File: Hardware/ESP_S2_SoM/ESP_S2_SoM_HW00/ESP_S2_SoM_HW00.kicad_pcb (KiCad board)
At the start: 6 copper layers, 29.5 x 24.7 mm, 59 parts, among them J101 DF40C-60DP-0.4V(51), J102 Bare PCB USB C, SW401 SW_Push, SW402 SW_Push, U201 BQ24075RGTR, U301 MIC5528-3.3YMT-T5, U401 ESP32-S2FH4, Y601 Crystal_GND24_Small

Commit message: exported pcb fab
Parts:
- removed G***: LOGO, Component_lib:puma_logo_14mm
- removed the J101 at (136.0, 106.2)
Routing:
- net IO8: track 11.5 -> 10.7 mm
- net SPI7: track 4.86 -> 4.16 mm

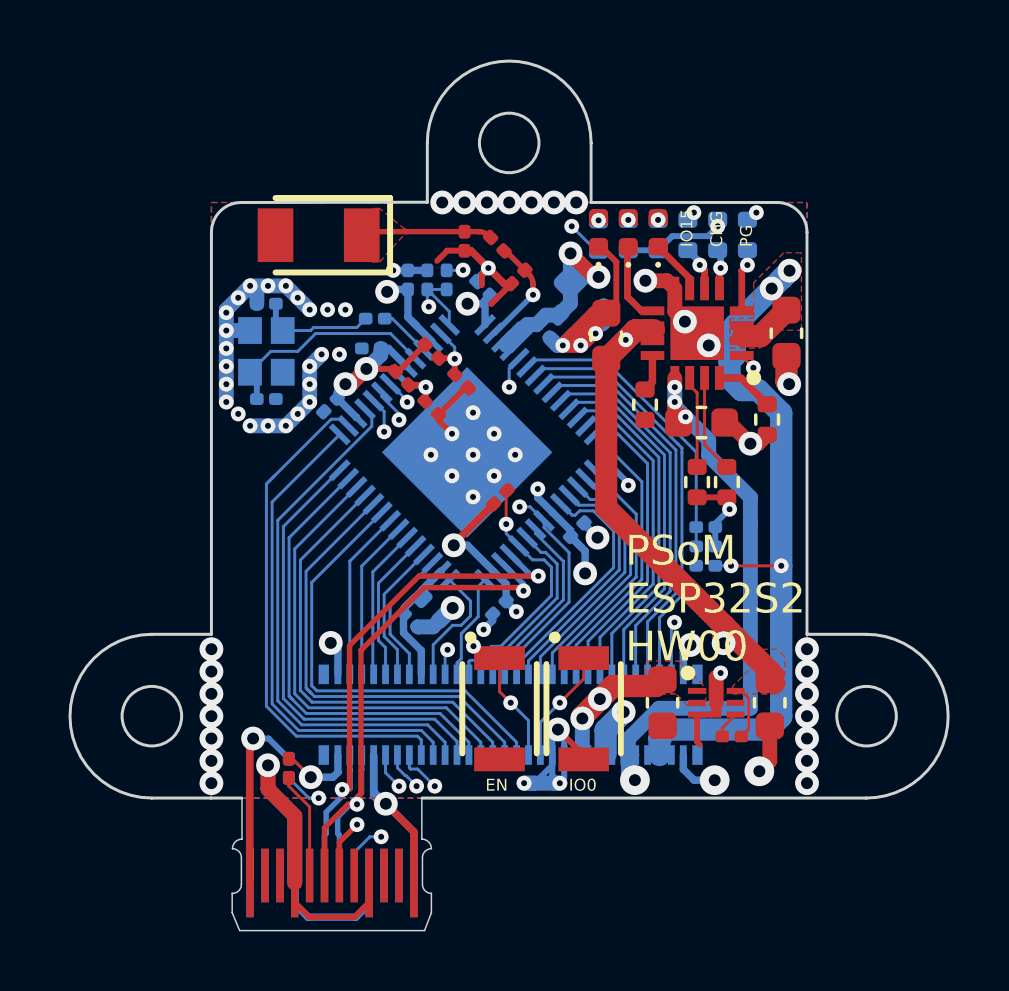
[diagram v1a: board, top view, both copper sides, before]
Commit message: updated prod files + holes are M1.6
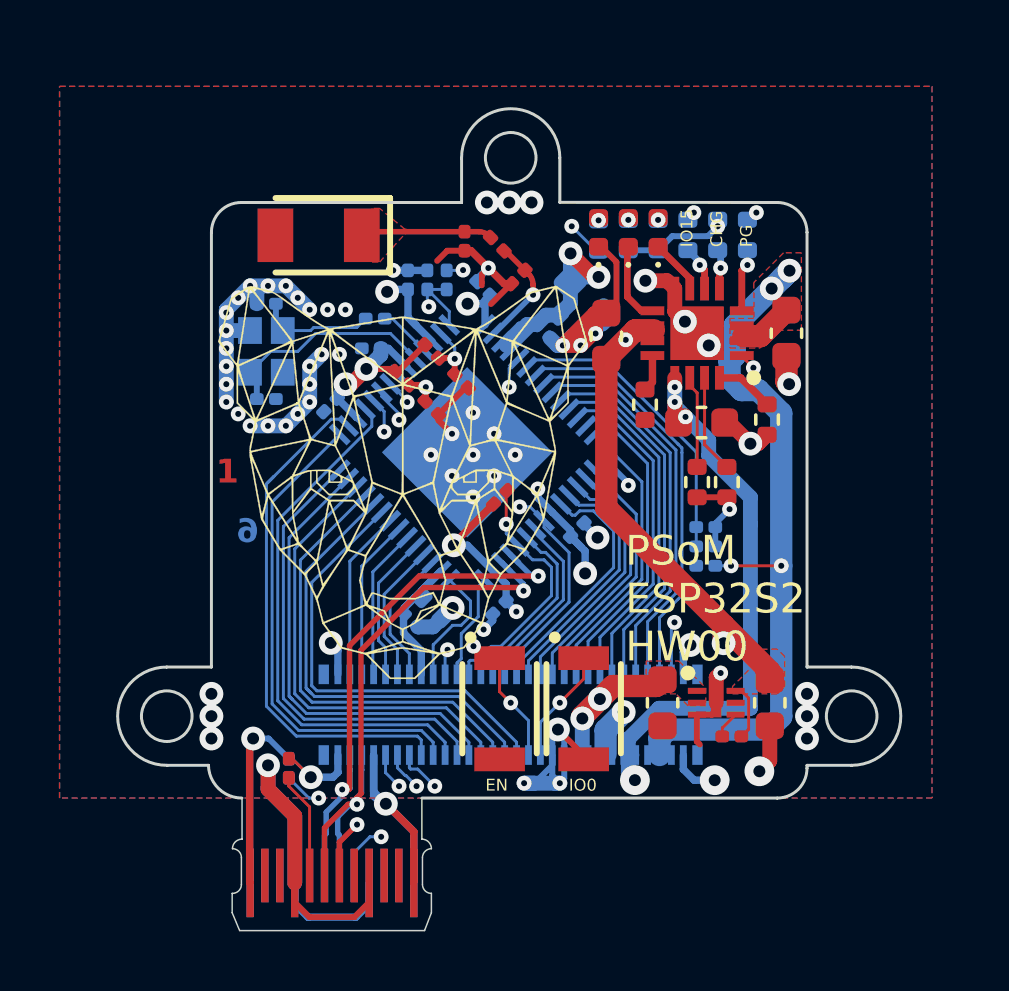
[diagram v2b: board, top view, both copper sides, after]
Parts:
- added G***: LOGO, Component_lib:puma_logo_14mm, F.Cu at (132.4, 98.4)
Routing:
- net GND: vias 83 -> 71
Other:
- board size 29.5 x 24.7 mm -> 26.3 x 23.1 mm
- board text added: "1"
- board text added: "2"
- board text added: "3"
- board text added: "4"
- board text added: "5"
- board text added: "6"

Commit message: Started PSoM RP2040
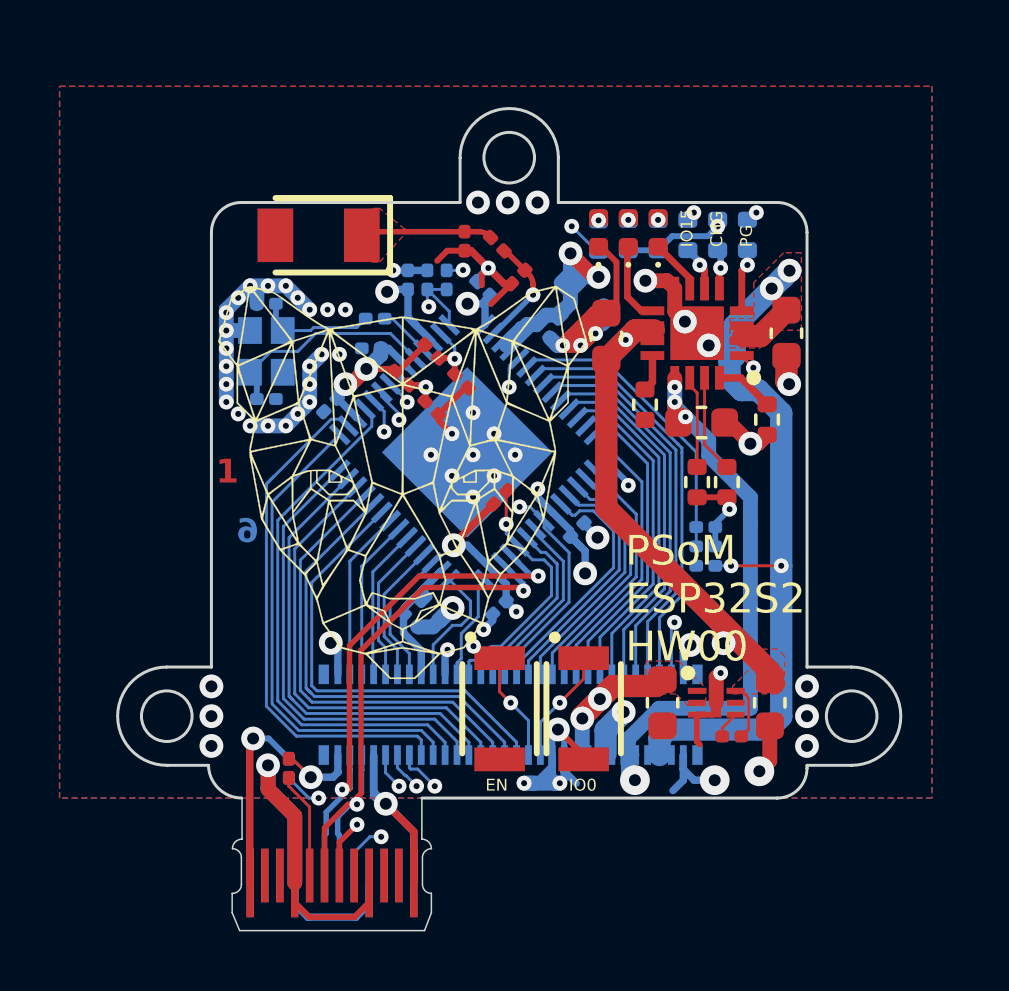
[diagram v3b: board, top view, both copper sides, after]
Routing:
- net GND: track 90.1 -> 94.2 mm
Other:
- board size 26.3 x 23.1 mm -> 26.3 x 23.2 mm

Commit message: made small mecha adjustement
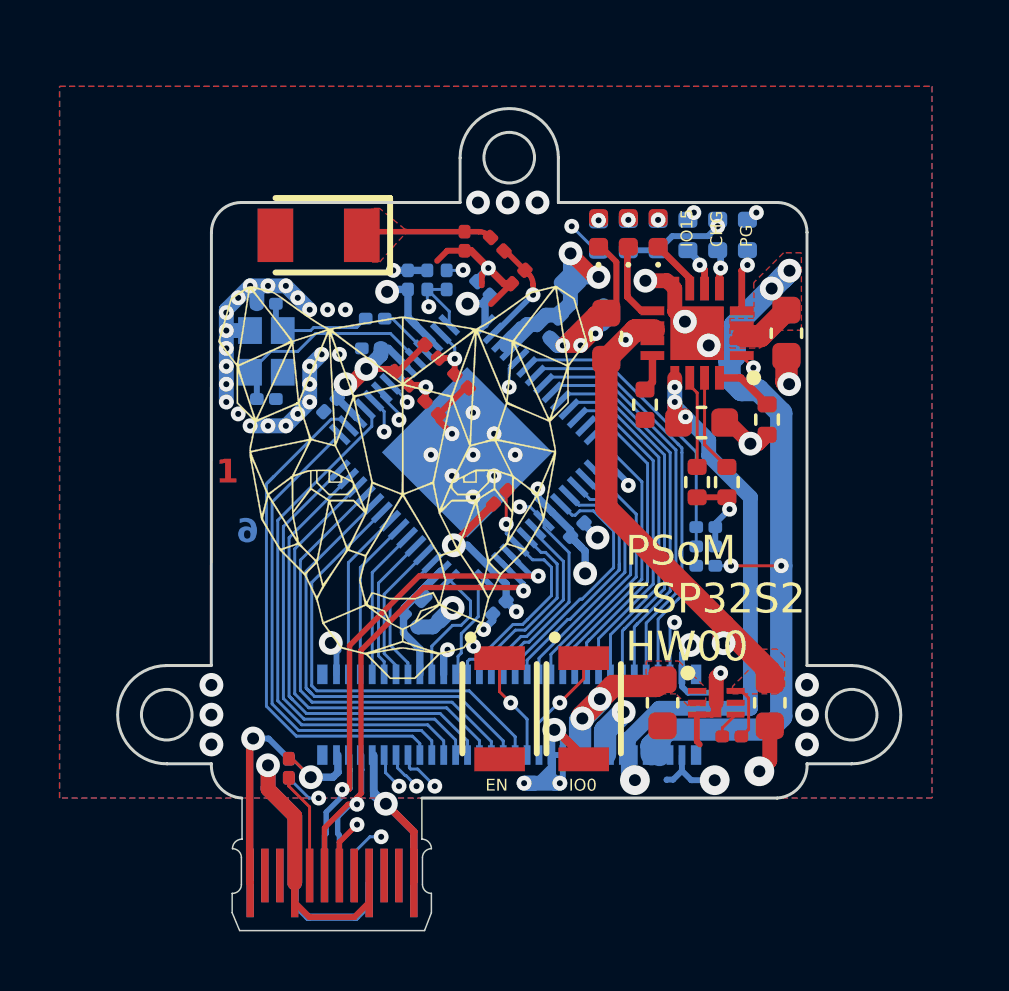
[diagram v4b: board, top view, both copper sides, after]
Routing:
- net GND: track 94.2 -> 96.0 mm
- net +3V3: track 35.4 -> 36.4 mm
- net /VBAT: track 26.2 -> 26.9 mm
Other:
- outline, holes or cut-outs redrawn

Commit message: final esp32s2 update?
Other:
- outline, holes or cut-outs redrawn
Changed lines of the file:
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@@
     )
   )
-  (gr_circle (center 124.05 106.25) (end 125.7 106.25)
+  (gr_circle (center 124.5 106.2) (end 126.15 106.2)
     (stroke (width 0.15) (type solid)) (fill solid) (layer "B.Mask"))
-  (gr_circle (center 136.05 87) (end 137.7 87)
+  (gr_circle (center 136 87.5) (end 137.65 87.5)
     (stroke (width 0.15) (type solid)) (fill solid) (layer "B.Mask"))
-  (gr_circle (center 148 106.25) (end 149.65 106.25)
+  (gr_circle (center 147.5 106.2) (end 149.15 106.2)
     (stroke (width 0.15) (type solid)) (fill solid) (layer "B.Mask"))
-  (gr_circle (center 136.05 87) (end 137.7 87)
+  (gr_circle (center 136 87.5) (end 137.65 87.5)
     (stroke (width 0.15) (type solid)) (fill solid) (layer "F.Mask"))
-  (gr_circle (center 136.05 87) (end 137.7 87)
+  (gr_circle (center 124.5 106.2) (end 126.15 106.2)
     (stroke (width 0.15) (type solid)) (fill solid) (layer "F.Mask"))
-  (gr_circle (center 124.05 106.25) (end 125.7 106.25)
-    (stroke (width 0.15) (type solid)) (fill solid) (layer "F.Mask"))
-  (gr_circle (center 148 106.25) (end 149.65 106.25)
+  (gr_circle (center 147.5 106.2) (end 149.15 106.2)
     (stroke (width 0.15) (type solid)) (fill solid) (layer "F.Mask"))
   (gr_line (start 145 89) (end 137.65 89)
     (stroke (width 0.1) (type default)) (layer "Edge.Cuts"))
-  (gr_line (start 124.5 104.54997) (end 125.994988 104.55)
+  (gr_line (start 124.5 104.55) (end 126 104.55)
     (stroke (width 0.1) (type default)) (layer "Edge.Cuts"))
   (gr_arc (start 145 89) (mid 145.707106 89.292893) (end 146 90)
     (stroke (width 0.1) (type default)) (layer "Edge.Cuts"))
-  (gr_arc (start 134.35 87.505012) (mid 135.995 85.844964) (end 137.650031 87.495012)
+  (gr_arc (start 134.35 87.5) (mid 136 85.85) (end 137.65 87.5)
     (stroke (width 0.1) (type default)) (layer "Edge.Cuts"))
-  (gr_arc (start 124.51 107.85) (mid 122.849954 106.205) (end 124.5 104.54997)
+  (gr_arc (start 124.5 107.85) (mid 122.85 106.2) (end 124.5 104.55)
     (stroke (width 0.1) (type default)) (layer "Edge.Cuts"))
-  (gr_arc (start 146 107.849985) (mid 145.738176 108.632099) (end 145 109)
+  (gr_arc (start 146 107.85) (mid 145.738173 108.632107) (end 145 109)
     (stroke (width 0.1) (type default)) (layer "Edge.Cuts"))
-  (gr_circle (center 124.5 106.2) (end 123.65 106.2)
+  (gr_circle (center 124.5 106.2) (end 125.35 106.2)
     (stroke (width 0.1) (type default)) (fill none) (layer "Edge.Cuts"))
-  (gr_line (start 147.489976 104.549985) (end 146 104.549985)
+  (gr_line (start 147.5 104.55) (end 146 104.55)
     (stroke (width 0.1) (type default)) (layer "Edge.Cuts"))
   (gr_line (start 134.35 89) (end 127 89)
     (stroke (width 0.1) (type default)) (layer "Edge.Cuts"))
-  (gr_circle (center 147.499977 106.199985) (end 148.349977 106.199985)
+  (gr_circle (center 147.5 106.2) (end 148.35 106.2)
     (stroke (width 0.1) (type default)) (fill none) (layer "Edge.Cuts"))
-  (gr_line (start 146 90) (end 146 104.549985)
+  (gr_line (start 146 90) (end 146 104.55)
     (stroke (width 0.1) (type default)) (layer "Edge.Cuts"))
-  (gr_line (start 125.994988 104.55) (end 126 90)
+  (gr_line (start 126 104.55) (end 126 90)
     (stroke (width 0.1) (type default)) (layer "Edge.Cuts"))
-  (gr_line (start 134.35 87.505012) (end 134.35 89)
+  (gr_line (start 134.35 87.5) (end 134.35 89)
     (stroke (width 0.1) (type default)) (layer "Edge.Cuts"))
-  (gr_line (start 146 107.849985) (end 147.499977 107.850015)
+  (gr_line (start 146 107.85) (end 147.5 107.85)
     (stroke (width 0.1) (type default)) (layer "Edge.Cuts"))
-  (gr_circle (center 136.000002 87.495012) (end 136.000001 86.645012)
+  (gr_circle (center 136 87.5) (end 136.85 87.5)
     (stroke (width 0.1) (type default)) (fill none) (layer "Edge.Cuts"))
   (gr_arc (start 127.026853 109) (mid 126.275244 108.637676) (end 126 107.85)
@@
   (gr_line (start 145 109) (end 133.066853 109)
     (stroke (width 0.1) (type default)) (layer "Edge.Cuts"))
-  (gr_line (start 137.650031 87.495012) (end 137.65 89)
+  (gr_line (start 137.65 87.5) (end 137.65 89)
     (stroke (width 0.1) (type default)) (layer "Edge.Cuts"))
   (gr_arc (start 126 90) (mid 126.292893 89.292894) (end 127 89)
     (stroke (width 0.1) (type default)) (layer "Edge.Cuts"))
-  (gr_line (start 124.51 107.85) (end 126 107.85)
+  (gr_line (start 124.5 107.85) (end 126 107.85)
     (stroke (width 0.1) (type default)) (layer "Edge.Cuts"))
-  (gr_arc (start 147.489976 104.549985) (mid 149.150023 106.194984) (end 147.499977 107.850015)
+  (gr_arc (start 147.5 104.55) (mid 149.15 106.2) (end 147.5 107.85)
     (stroke (width 0.1) (type default)) (layer "Edge.Cuts"))
   (gr_text "1" (at 126.15 98.5) (layer "F.Cu")
